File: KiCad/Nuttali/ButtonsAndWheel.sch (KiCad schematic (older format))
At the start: 23 parts

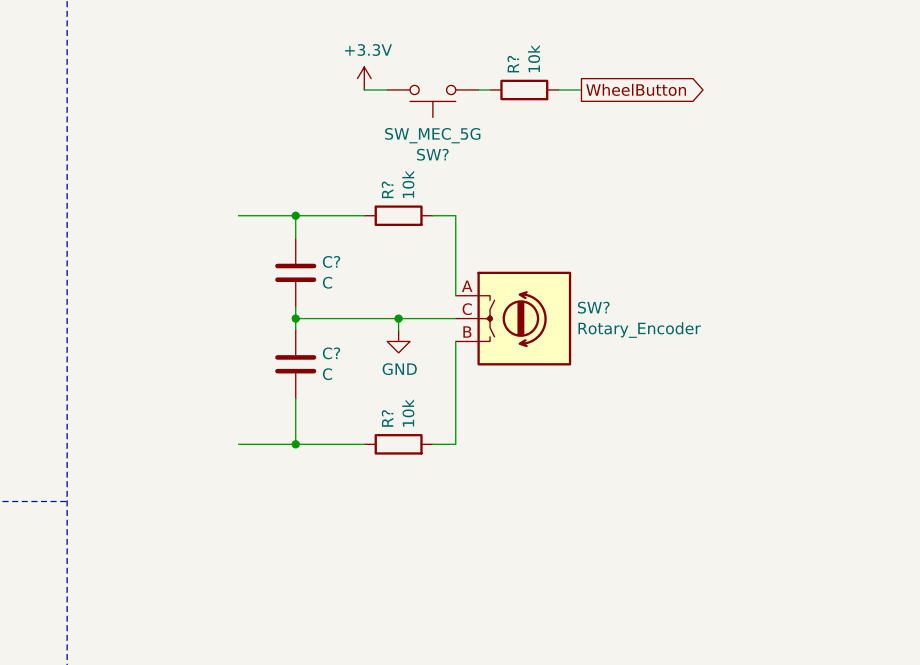
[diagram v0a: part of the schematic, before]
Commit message: Added scroolWheel and rgb
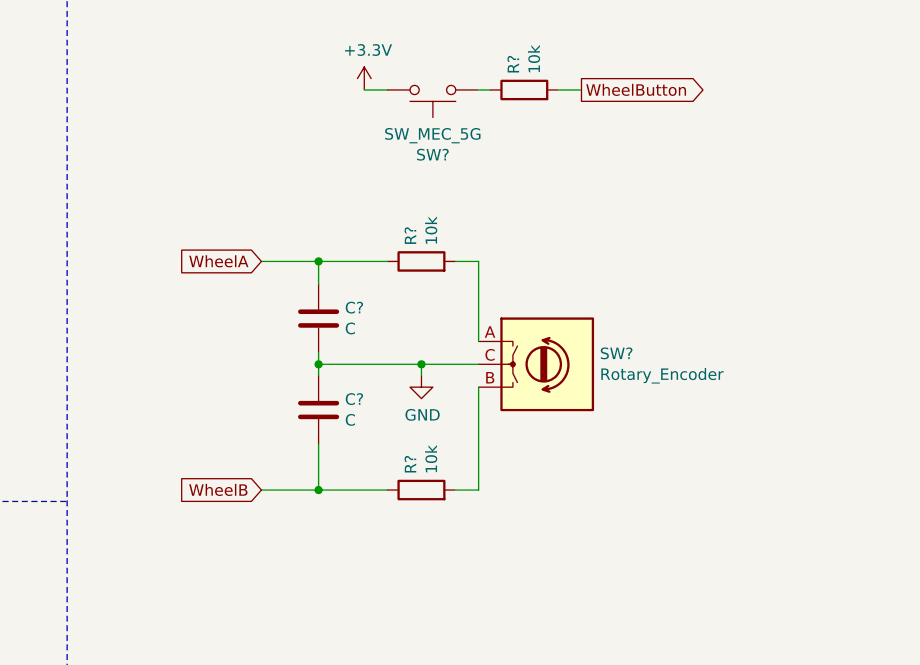
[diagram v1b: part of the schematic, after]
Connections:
- net labels added: WheelA, WheelB
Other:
- moved on the sheet: C?, R?, SW?
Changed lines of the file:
@@
 L Device:Rotary_Encoder SW?
 U 1 1 60310A0D
-P 5100 3450
-F 0 "SW?" H 5330 3496 50  0000 L CNN
-F 1 "Rotary_Encoder" H 5330 3405 50  0000 L CNN
-F 2 "" H 4950 3610 50  0001 C CNN
-F 3 "~" H 5100 3710 50  0001 C CNN
-	1    5100 3450
+P 5200 3650
+F 0 "SW?" H 5430 3696 50  0000 L CNN
+F 1 "Rotary_Encoder" H 5430 3605 50  0000 L CNN
+F 2 "" H 5050 3810 50  0001 C CNN
+F 3 "~" H 5200 3910 50  0001 C CNN
+	1    5200 3650
 	1    0    0    -1
 $EndComp
@@
 L Device:C C?
 U 1 1 60318A18
-P 4100 3250
-F 0 "C?" H 4215 3296 50  0000 L CNN
-F 1 "C" H 4215 3205 50  0000 L CNN
-F 2 "" H 4138 3100 50  0001 C CNN
-F 3 "~" H 4100 3250 50  0001 C CNN
-	1    4100 3250
+P 4200 3450
+F 0 "C?" H 4315 3496 50  0000 L CNN
+F 1 "C" H 4315 3405 50  0000 L CNN
+F 2 "" H 4238 3300 50  0001 C CNN
+F 3 "~" H 4200 3450 50  0001 C CNN
+	1    4200 3450
 	1    0    0    -1
 $EndComp
@@
 L Device:C C?
 U 1 1 6031913E
-P 4100 3650
-F 0 "C?" H 4215 3696 50  0000 L CNN
-F 1 "C" H 4215 3605 50  0000 L CNN
-F 2 "" H 4138 3500 50  0001 C CNN
-F 3 "~" H 4100 3650 50  0001 C CNN
-	1    4100 3650
+P 4200 3850
+F 0 "C?" H 4315 3896 50  0000 L CNN
+F 1 "C" H 4315 3805 50  0000 L CNN
+F 2 "" H 4238 3700 50  0001 C CNN
+F 3 "~" H 4200 3850 50  0001 C CNN
+	1    4200 3850
 	1    0    0    -1
 $EndComp
@@
 L Device:R R?
 U 1 1 6031998E
-P 4550 3000
-F 0 "R?" H 4620 3046 50  0000 L CNN
-F 1 "10k" H 4620 2955 50  0000 L CNN
-F 2 "" V 4480 3000 50  0001 C CNN
-F 3 "~" H 4550 3000 50  0001 C CNN
-	1    4550 3000
+P 4650 3200
+F 0 "R?" H 4720 3246 50  0000 L CNN
+F 1 "10k" H 4720 3155 50  0000 L CNN
+F 2 "" V 4580 3200 50  0001 C CNN
+F 3 "~" H 4650 3200 50  0001 C CNN
+	1    4650 3200
 	0    -1   -1   0
 $EndComp
@@
 L Device:R R?
 U 1 1 6031A38F
-P 4550 4000
-F 0 "R?" H 4620 4046 50  0000 L CNN
-F 1 "10k" H 4620 3955 50  0000 L CNN
-F 2 "" V 4480 4000 50  0001 C CNN
-F 3 "~" H 4550 4000 50  0001 C CNN
-	1    4550 4000
+P 4650 4200
+F 0 "R?" H 4720 4246 50  0000 L CNN
+F 1 "10k" H 4720 4155 50  0000 L CNN
+F 2 "" V 4580 4200 50  0001 C CNN
+F 3 "~" H 4650 4200 50  0001 C CNN
+	1    4650 4200
 	0    -1   -1   0
 $EndComp
 Wire Wire Line
-	4800 3350 4800 3000
+	4900 3550 4900 3200
 Wire Wire Line
-	4800 3000 4700 3000
+	4900 3200 4800 3200
 Wire Wire Line
-	4400 3000 4100 3000
+	4500 3200 4200 3200
 Wire Wire Line
-	4100 3000 4100 3100
+	4200 3200 4200 3300
 Wire Wire Line
-	4100 3000 3850 3000
-Connection ~ 4100 3000
+	4200 3200 3950 3200
+Connection ~ 4200 3200
 Wire Wire Line
-	4800 3550 4800 4000
+	4900 3750 4900 4200
 Wire Wire Line
-	4800 4000 4700 4000
+	4900 4200 4800 4200
 Wire Wire Line
-	4400 4000 4100 4000
+	4500 4200 4200 4200
 Wire Wire Line
-	4100 4000 4100 3800
+	4200 4200 4200 4000
 Wire Wire Line
-	4100 4000 3850 4000
-Connection ~ 4100 4000
+	4200 4200 3950 4200
+Connection ~ 4200 4200
 Wire Wire Line
-	4100 3400 4100 3450
+	4200 3600 4200 3650
 Wire Wire Line
-	4100 3450 4550 3450
-Connection ~ 4100 3450
+	4200 3650 4650 3650
+Connection ~ 4200 3650
 Wire Wire Line
-	4100 3450 4100 3500
+	4200 3650 4200 3700
 Wire Wire Line
-	4550 3450 4550 3500
-Connection ~ 4550 3450
+	4650 3650 4650 3700
+Connection ~ 4650 3650
 Wire Wire Line
-	4550 3450 4800 3450
+	4650 3650 4900 3650
 $Comp
 L power:GND #PWR?
 U 1 1 6032A748
-P 4550 3500
-F 0 "#PWR?" H 4550 3250 50  0001 C CNN
-F 1 "GND" H 4555 3327 50  0000 C CNN
-F 2 "" H 4550 3500 50  0001 C CNN
-F 3 "" H 4550 3500 50  0001 C CNN
-	1    4550 3500
+P 4650 3700
+F 0 "#PWR?" H 4650 3450 50  0001 C CNN
+F 1 "GND" H 4655 3527 50  0000 C CNN
+F 2 "" H 4650 3700 50  0001 C CNN
+F 3 "" H 4650 3700 50  0001 C CNN
+	1    4650 3700
 	1    0    0    -1
 $EndComp
+Text GLabel 3950 3200 0    50   Input ~ 0
+WheelA
+Text GLabel 3950 4200 0    50   Input ~ 0
+WheelB
 $EndSCHEMATC

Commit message: some footprints fixed
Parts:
- C27, C28, C29, C30: renamed from C?; footprint (none) -> Capacitor_SMD:C_0805_2012Metric_Pad1.18x1.45mm_HandSolder; symbol Device:C -> Nuttali-rescue:C-Device
- D3, D4: renamed from D?; symbol Device:LED -> Nuttali-rescue:LED-Device
- R10, R11, R12, R13, R14, R15, R7, R8, R9: renamed from R?; footprint (none) -> Resistor_SMD:R_0815_2038Metric_Pad1.20x4.05mm_HandSolder; symbol Device:R -> Nuttali-rescue:R-Device
- SW10, SW3, SW4, SW5, SW6, SW7, SW9: renamed from SW?; symbol Switch:SW_MEC_5G -> Nuttali-rescue:SW_MEC_5G-Switch
- SW8: renamed from SW?; symbol Device:Rotary_Encoder -> Nuttali-rescue:Rotary_Encoder-Device
